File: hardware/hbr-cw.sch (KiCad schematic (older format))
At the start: 39 parts, among them J1 ON/OFF, J10 BluePill_Right, J11 MAIN, J12 BAND, J13 LCD 0802, J14 RIT/XIT, J15 FAST, J16 LOCK, J17 RFAMP, J18 CLAR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

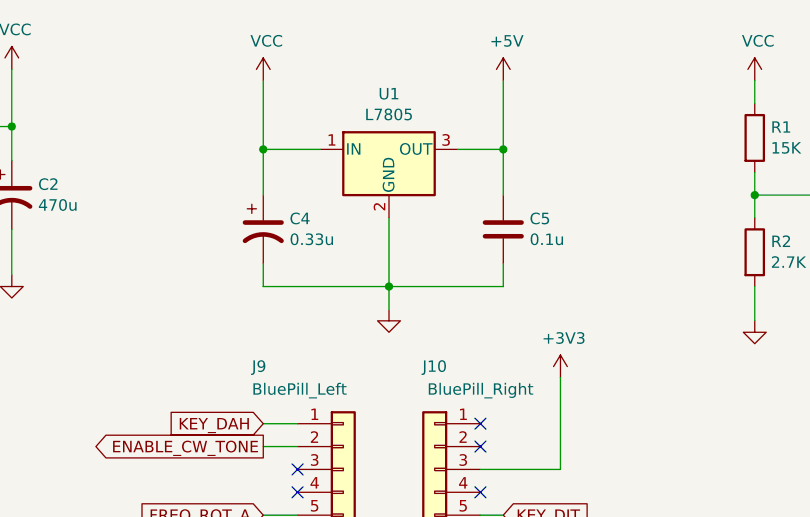
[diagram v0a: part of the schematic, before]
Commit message: Add a warning that U1 can get a little hot + minor changes
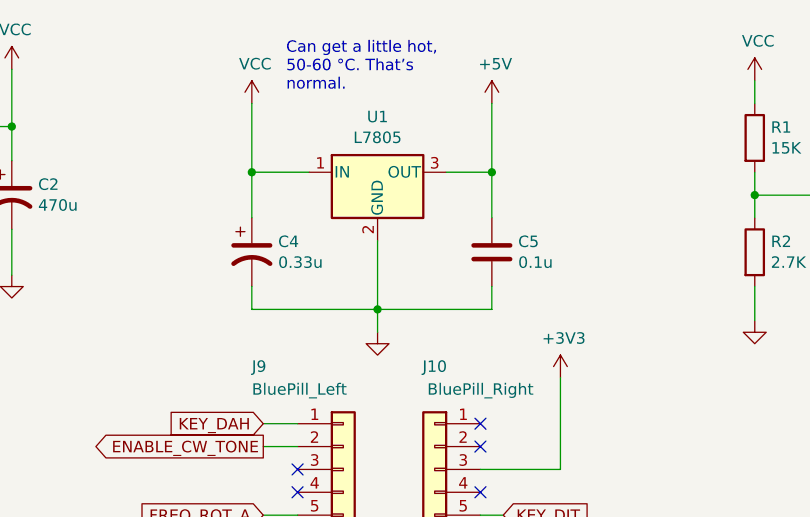
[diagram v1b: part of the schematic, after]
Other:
- note added: "Can get a little hot, \n50-60 °C. That’s\nnormal."
- moved on the sheet: C4, C5, U1
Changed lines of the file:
@@
 L power:VCC #PWR02
 U 1 1 61D219EF
-P 5100 800
-F 0 "#PWR02" H 5100 650 50  0001 C CNN
-F 1 "VCC" H 5115 973 50  0000 C CNN
-F 2 "" H 5100 800 50  0001 C CNN
-F 3 "" H 5100 800 50  0001 C CNN
-	1    5100 800
+P 5050 900
+F 0 "#PWR02" H 5050 750 50  0001 C CNN
+F 1 "VCC" H 5065 1073 50  0000 C CNN
+F 2 "" H 5050 900 50  0001 C CNN
+F 3 "" H 5050 900 50  0001 C CNN
+	1    5050 900
 	1    0    0    -1
 $EndComp
@@
 L Device:CP1 C4
 U 1 1 61D21DE5
-P 5100 1450
-F 0 "C4" H 5215 1496 50  0000 L CNN
-F 1 "0.33u" H 5215 1405 50  0000 L CNN
-F 2 "Capacitor_THT:C_Radial_D5.0mm_H5.0mm_P2.00mm" H 5100 1450 50  0001 C CNN
-F 3 "~" H 5100 1450 50  0001 C CNN
-	1    5100 1450
+P 5050 1550
+F 0 "C4" H 5165 1596 50  0000 L CNN
+F 1 "0.33u" H 5165 1505 50  0000 L CNN
+F 2 "Capacitor_THT:C_Radial_D5.0mm_H5.0mm_P2.00mm" H 5050 1550 50  0001 C CNN
+F 3 "~" H 5050 1550 50  0001 C CNN
+	1    5050 1550
 	1    0    0    -1
 $EndComp
@@
 L Device:C C5
 U 1 1 61D22656
-P 6150 1450
-F 0 "C5" H 6265 1496 50  0000 L CNN
-F 1 "0.1u" H 6265 1405 50  0000 L CNN
-F 2 "Capacitor_SMD:C_0805_2012Metric_Pad1.15x1.40mm_HandSolder" H 6188 1300 50  0001 C CNN
-F 3 "~" H 6150 1450 50  0001 C CNN
-	1    6150 1450
+P 6100 1550
+F 0 "C5" H 6215 1596 50  0000 L CNN
+F 1 "0.1u" H 6215 1505 50  0000 L CNN
+F 2 "Capacitor_SMD:C_0805_2012Metric_Pad1.15x1.40mm_HandSolder" H 6138 1400 50  0001 C CNN
+F 3 "~" H 6100 1550 50  0001 C CNN
+	1    6100 1550
 	1    0    0    -1
 $EndComp
@@
 L power:GND #PWR013
 U 1 1 61D22A88
-P 5650 1800
-F 0 "#PWR013" H 5650 1550 50  0001 C CNN
-F 1 "GND" H 5655 1627 50  0001 C CNN
-F 2 "" H 5650 1800 50  0001 C CNN
-F 3 "" H 5650 1800 50  0001 C CNN
-	1    5650 1800
+P 5600 1900
+F 0 "#PWR013" H 5600 1650 50  0001 C CNN
+F 1 "GND" H 5605 1727 50  0001 C CNN
+F 2 "" H 5600 1900 50  0001 C CNN
+F 3 "" H 5600 1900 50  0001 C CNN
+	1    5600 1900
 	1    0    0    -1
 $EndComp
@@
 L power:+5V #PWR03
 U 1 1 61D23373
-P 6150 800
-F 0 "#PWR03" H 6150 650 50  0001 C CNN
-F 1 "+5V" H 6165 973 50  0000 C CNN
-F 2 "" H 6150 800 50  0001 C CNN
-F 3 "" H 6150 800 50  0001 C CNN
-	1    6150 800
-	1    0    0    -1
-$EndComp
-Wire Wire Line
-	5100 800  5100 1100
-Wire Wire Line
-	5350 1100 5100 1100
-Connection ~ 5100 1100
-Wire Wire Line
-	5100 1100 5100 1300
-Wire Wire Line
-	5650 1400 5650 1700
-Wire Wire Line
-	5100 1600 5100 1700
-Wire Wire Line
-	5100 1700 5650 1700
-Connection ~ 5650 1700
-Wire Wire Line
-	5650 1700 5650 1800
-Wire Wire Line
-	5650 1700 6150 1700
-Wire Wire Line
-	6150 1100 5950 1100
-Wire Wire Line
-	6150 1100 6150 800
+P 6100 900
+F 0 "#PWR03" H 6100 750 50  0001 C CNN
+F 1 "+5V" H 6115 1073 50  0000 C CNN
+F 2 "" H 6100 900 50  0001 C CNN
+F 3 "" H 6100 900 50  0001 C CNN
+	1    6100 900
+	1    0    0    -1
+$EndComp
+Wire Wire Line
+	5050 900  5050 1200
+Wire Wire Line
+	5300 1200 5050 1200
+Connection ~ 5050 1200
+Wire Wire Line
+	5050 1200 5050 1400
+Wire Wire Line
+	5600 1500 5600 1800
+Wire Wire Line
+	5050 1700 5050 1800
+Wire Wire Line
+	5050 1800 5600 1800
+Connection ~ 5600 1800
+Wire Wire Line
+	5600 1800 5600 1900
+Wire Wire Line
+	5600 1800 6100 1800
+Wire Wire Line
+	6100 1200 5900 1200
+Wire Wire Line
+	6100 1200 6100 900
 Wire Wire Line
 	4000 1000 4000 1150
@@
 	5100 3200 5250 3200
 Wire Wire Line
-	6150 1700 6150 1600
-Wire Wire Line
-	6150 1300 6150 1100
-Connection ~ 6150 1100
+	6100 1800 6100 1700
+Wire Wire Line
+	6100 1400 6100 1200
+Connection ~ 6100 1200
 Text Notes 3750 7050 0    50   ~ 0
 The Si5351 module has built-in\npull-up resistors for the I2C bus.
@@
 L Regulator_Linear:L7805 U?
 U 1 1 62D34BEE
-P 5650 1100
+P 5600 1200
 AR Path="/621694F4/62D34BEE" Ref="U?"  Part="1"
 AR Path="/61F4800D/62D34BEE" Ref="U?"  Part="1"
 AR Path="/62D34BEE" Ref="U1"  Part="1"
-F 0 "U1" H 5650 1342 50  0000 C CNN
-F 1 "L7805" H 5650 1251 50  0000 C CNN
-F 2 "Package_TO_SOT_SMD:TO-263-2" H 5675 950 50  0001 L CIN
-F 3 "" H 5650 1050 50  0001 C CNN
-	1    5650 1100
+F 0 "U1" H 5600 1442 50  0000 C CNN
+F 1 "L7805" H 5600 1351 50  0000 C CNN
+F 2 "Package_TO_SOT_SMD:TO-263-2" H 5625 1050 50  0001 L CIN
+F 3 "" H 5600 1150 50  0001 C CNN
+	1    5600 1200
 	1    0    0    -1
 $EndComp
@@
 Wire Wire Line
 	10200 4550 10200 4750
+Text Notes 5200 850  0    50   ~ 0
+Can get a little hot, \n50-60 °C. That’s\nnormal.
 $EndSCHEMATC
